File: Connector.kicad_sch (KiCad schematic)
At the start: 1 part, among them J6 2-338069-0

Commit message: Стартовый вариант
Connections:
- net HIN_A: now reaches J6.1
- net LIN_B: now reaches J6.10
- net HIN_B: now reaches J6.11
- net LIN_C: now reaches J6.19
- net LIN_A: now reaches J6.2
- net HIN_C: now reaches J6.20
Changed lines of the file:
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@@
 (kicad_sch (version 20230121) (generator eeschema)
   (paper "A4")
+  (global_label "HIN_C" (shape input) (at 132.08 111.76 180) (fields_autoplaced)
+    (effects (font (size 1.27 1.27)) (justify right))
+    (property "Intersheetrefs" "${INTERSHEET_REFS}" (at 123.5914 111.76 0)
+      (effects (font (size 1.27 1.27)) (justify right) hide)
+    )
+  )
+  (global_label "LIN_B" (shape input) (at 132.08 86.36 180) (fields_autoplaced)
+    (effects (font (size 1.27 1.27)) (justify right))
+    (property "Intersheetrefs" "${INTERSHEET_REFS}" (at 123.8938 86.36 0)
+      (effects (font (size 1.27 1.27)) (justify right) hide)
+    )
+  )
+  (global_label "LIN_C" (shape input) (at 132.08 109.22 180) (fields_autoplaced)
+    (effects (font (size 1.27 1.27)) (justify right))
+    (property "Intersheetrefs" "${INTERSHEET_REFS}" (at 123.8938 109.22 0)
+      (effects (font (size 1.27 1.27)) (justify right) hide)
+    )
+  )
+  (global_label "HIN_A" (shape input) (at 132.08 63.5 180) (fields_autoplaced)
+    (effects (font (size 1.27 1.27)) (justify right))
+    (property "Intersheetrefs" "${INTERSHEET_REFS}" (at 123.7728 63.5 0)
+      (effects (font (size 1.27 1.27)) (justify right) hide)
+    )
+  )
+  (global_label "HIN_B" (shape input) (at 132.08 88.9 180) (fields_autoplaced)
+    (effects (font (size 1.27 1.27)) (justify right))
+    (property "Intersheetrefs" "${INTERSHEET_REFS}" (at 123.5914 88.9 0)
+      (effects (font (size 1.27 1.27)) (justify right) hide)
+    )
+  )
+  (global_label "LIN_A" (shape input) (at 132.08 66.04 180) (fields_autoplaced)
+    (effects (font (size 1.27 1.27)) (justify right))
+    (property "Intersheetrefs" "${INTERSHEET_REFS}" (at 124.0752 66.04 0)
+      (effects (font (size 1.27 1.27)) (justify right) hide)
+    )
+  )
   (symbol (lib_id "Connector_My:2-338069-0") (at 132.08 63.5 0) (unit 1)
     (in_bom yes) (on_board yes) (dnp no) (fields_autoplaced)

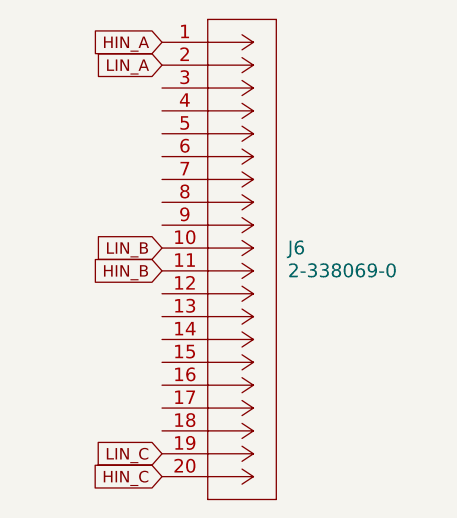
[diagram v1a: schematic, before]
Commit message: Добавил шунты
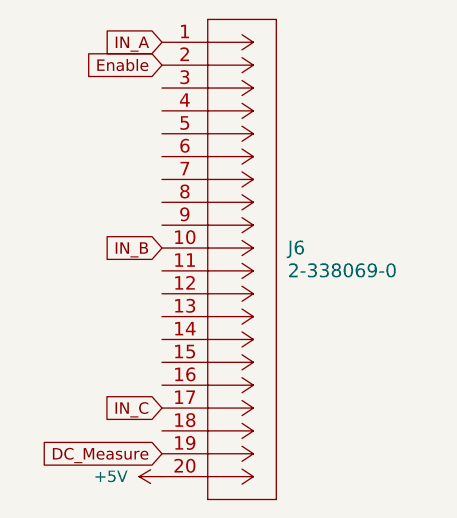
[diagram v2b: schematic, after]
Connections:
- net IN_C: now reaches J6.17
- net HIN_A renamed IN_A
- net HIN_B: no longer names the net of J6.11
- net HIN_C renamed +5V
- net LIN_A renamed Enable
- net LIN_B renamed IN_B
- net LIN_C renamed DC_Measure
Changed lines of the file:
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@@
 (kicad_sch (version 20230121) (generator eeschema)
   (paper "A4")
-  (global_label "HIN_C" (shape input) (at 132.08 111.76 180) (fields_autoplaced)
+  (global_label "DC_Measure" (shape input) (at 132.08 109.22 180) (fields_autoplaced)
     (effects (font (size 1.27 1.27)) (justify right))
-    (property "Intersheetrefs" "${INTERSHEET_REFS}" (at 123.5914 111.76 0)
+    (property "Intersheetrefs" "${INTERSHEET_REFS}" (at 117.8463 109.22 0)
       (effects (font (size 1.27 1.27)) (justify right) hide)
     )
   )
-  (global_label "LIN_B" (shape input) (at 132.08 86.36 180) (fields_autoplaced)
+  (global_label "IN_C" (shape input) (at 132.08 104.14 180) (fields_autoplaced)
     (effects (font (size 1.27 1.27)) (justify right))
-    (property "Intersheetrefs" "${INTERSHEET_REFS}" (at 123.8938 86.36 0)
+    (property "Intersheetrefs" "${INTERSHEET_REFS}" (at 124.9219 104.14 0)
       (effects (font (size 1.27 1.27)) (justify right) hide)
     )
   )
-  (global_label "LIN_C" (shape input) (at 132.08 109.22 180) (fields_autoplaced)
+  (global_label "Enable" (shape input) (at 132.08 66.04 180) (fields_autoplaced)
     (effects (font (size 1.27 1.27)) (justify right))
-    (property "Intersheetrefs" "${INTERSHEET_REFS}" (at 123.8938 109.22 0)
+    (property "Intersheetrefs" "${INTERSHEET_REFS}" (at 122.745 66.04 0)
       (effects (font (size 1.27 1.27)) (justify right) hide)
     )
   )
-  (global_label "HIN_A" (shape input) (at 132.08 63.5 180) (fields_autoplaced)
+  (global_label "IN_A" (shape input) (at 132.08 63.5 180) (fields_autoplaced)
     (effects (font (size 1.27 1.27)) (justify right))
-    (property "Intersheetrefs" "${INTERSHEET_REFS}" (at 123.7728 63.5 0)
+    (property "Intersheetrefs" "${INTERSHEET_REFS}" (at 125.1033 63.5 0)
       (effects (font (size 1.27 1.27)) (justify right) hide)
     )
   )
-  (global_label "HIN_B" (shape input) (at 132.08 88.9 180) (fields_autoplaced)
+  (global_label "IN_B" (shape input) (at 132.08 86.36 180) (fields_autoplaced)
     (effects (font (size 1.27 1.27)) (justify right))
-    (property "Intersheetrefs" "${INTERSHEET_REFS}" (at 123.5914 88.9 0)
+    (property "Intersheetrefs" "${INTERSHEET_REFS}" (at 124.9219 86.36 0)
       (effects (font (size 1.27 1.27)) (justify right) hide)
     )
   )
-  (global_label "LIN_A" (shape input) (at 132.08 66.04 180) (fields_autoplaced)
-    (effects (font (size 1.27 1.27)) (justify right))
-    (property "Intersheetrefs" "${INTERSHEET_REFS}" (at 124.0752 66.04 0)
-      (effects (font (size 1.27 1.27)) (justify right) hide)
+  (symbol (lib_id "power:+5V") (at 132.08 111.76 90) (unit 1)
+    (in_bom yes) (on_board yes) (dnp no) (fields_autoplaced)
+    (property "Reference" "#PWR010" (at 135.89 111.76 0)
+      (effects (font (size 1.27 1.27)) hide)
+    )
+    (property "Value" "+5V" (at 128.27 111.76 90)
+      (effects (font (size 1.27 1.27)) (justify left))
+    )
+    (property "Footprint" "" (at 132.08 111.76 0)
+      (effects (font (size 1.27 1.27)) hide)
+    )
+    (property "Datasheet" "" (at 132.08 111.76 0)
+      (effects (font (size 1.27 1.27)) hide)
+    )
+    (pin "1")
+    (instances
+      (project "Силовая плата"
+        (path "/96c6fc92-8ec6-44f7-b0dc-9ad8f1acea09"
+          (reference "#PWR010") (unit 1)
+        )
+        (path "/96c6fc92-8ec6-44f7-b0dc-9ad8f1acea09/1efb5faf-bb82-4ac6-a144-d6576b4720aa"
+          (reference "#PWR03") (unit 1)
+        )
+        (path "/96c6fc92-8ec6-44f7-b0dc-9ad8f1acea09/a27b443f-c036-4fd6-934c-6ea912709de0"
+          (reference "#PWR09") (unit 1)
+        )
+      )
     )
   )

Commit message: Стартовый вариант
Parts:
- removed J6: 2-338069-0, Connector_My:2-338069-0, symbol Connector_My:2-338069-0

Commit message: Стартовая версия
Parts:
- added J6: Conn_02x04_Odd_Even, Connector_PinHeader_2.54mm:PinHeader_2x04_P2.54mm_Vertical, symbol Connector_Generic:Conn_02x04_Odd_Even
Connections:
- net +12V: now also J6.4 (Pin_4)
- net +5V: now also J6.6 (Pin_6)
- net DC_Measure: now also J6.8 (Pin_8)
- net Enable: now also J6.7 (Pin_7)
- net GND: now also J6.2 (Pin_2)
- net IN_A: now also J6.1 (Pin_1)
- net IN_B: now also J6.3 (Pin_3)
- net IN_C: now also J6.5 (Pin_5)

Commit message: Стартовая версия
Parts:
- removed J6: Conn_02x04_Odd_Even, Connector_PinHeader_2.54mm:PinHeader_2x04_P2.54mm_Vertical, symbol Connector_Generic:Conn_02x04_Odd_Even
- added J6: B_CTRL, Connector_PinSocket_2.54mm:PinSocket_2x02_P2.54mm_Vertical_SMD, symbol Connector_Generic:Conn_02x02_Odd_Even
- added J7: A_CTRL, Connector_PinSocket_2.54mm:PinSocket_2x04_P2.54mm_Vertical_SMD, symbol Connector_Generic:Conn_02x04_Odd_Even
- added J9: C_CTRL, Connector_PinSocket_2.54mm:PinSocket_2x04_P2.54mm_Vertical_SMD, symbol Connector_Generic:Conn_02x04_Odd_Even
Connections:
- net +5V: now also J9.7 (Pin_7)
- net DC_Measure: now also J9.5 (Pin_5)
- net GND: now also J6.4 (Pin_4), J7.4 (Pin_4), J7.6 (Pin_6), J7.8 (Pin_8), J9.4 (Pin_4), J9.6 (Pin_6), J9.8 (Pin_8)
- new net +24V: J7.5 (Pin_5)
- new net A: J7.3 (Pin_3)
- new net B: J6.3 (Pin_3)
- new net C: J9.3 (Pin_3)
- new net G1: J7.1 (Pin_1)
- new net G2: J7.2 (Pin_2)
- new net G3: J6.1 (Pin_1)
- new net G4: J6.2 (Pin_2)
- new net G5: J9.1 (Pin_1)
- new net G6: J9.2 (Pin_2)
- new net Temp_out: J7.7 (Pin_7)

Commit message: Стартовая версия
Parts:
- removed J6: B_CTRL, Connector_PinSocket_2.54mm:PinSocket_2x02_P2.54mm_Vertical_SMD, symbol Connector_Generic:Conn_02x02_Odd_Even
- removed J7: A_CTRL, Connector_PinSocket_2.54mm:PinSocket_2x04_P2.54mm_Vertical_SMD, symbol Connector_Generic:Conn_02x04_Odd_Even
- removed J9: C_CTRL, Connector_PinSocket_2.54mm:PinSocket_2x04_P2.54mm_Vertical_SMD, symbol Connector_Generic:Conn_02x04_Odd_Even
- added J6: Conn_01x04, Connector_PinHeader_2.54mm:PinHeader_1x04_P2.54mm_Vertical, symbol Connector_Generic:Conn_01x04
- added J9: Conn_01x08, Connector_PinHeader_2.54mm:PinHeader_1x08_P2.54mm_Vertical, symbol Connector_Generic:Conn_01x08
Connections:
- net A: now also J6.2 (Pin_2)
- net B: now also J9.8 (Pin_8)
- net C: now also J9.4 (Pin_4)
- net G1: now also J6.1 (Pin_1)
- net G2: now also J6.3 (Pin_3)
- net G3: now also J9.7 (Pin_7)
- net G4: now also J9.5 (Pin_5)
- net G5: now also J9.3 (Pin_3)
- net G6: now also J9.1 (Pin_1)
- net GND: now also J6.4 (Pin_4), J9.2 (Pin_2), J9.6 (Pin_6)

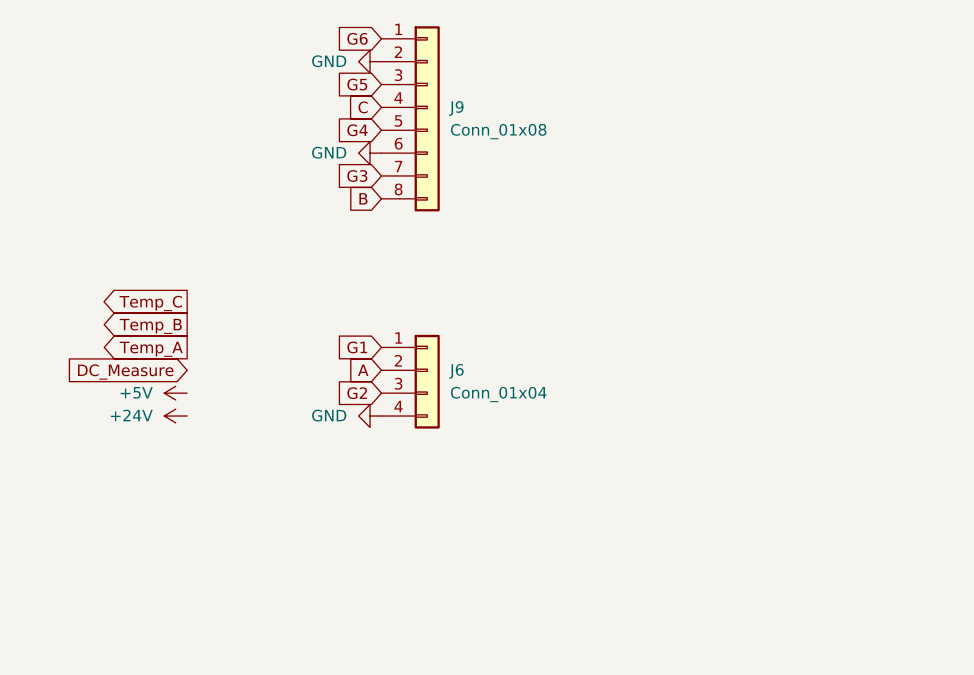
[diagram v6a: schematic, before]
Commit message: Перенес защиту от переполюсовки и добавил керамику
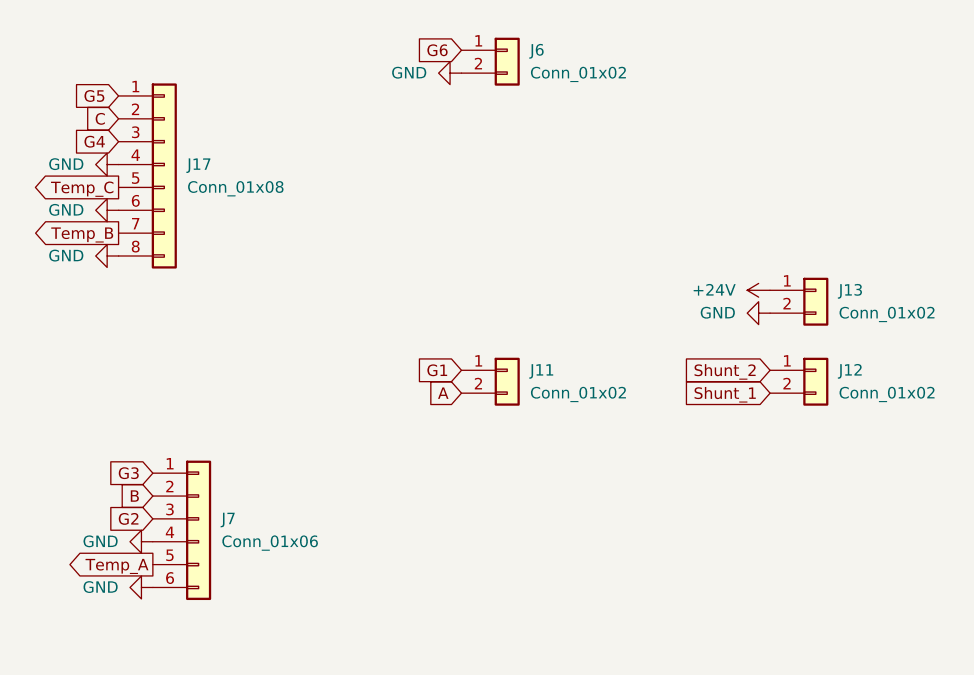
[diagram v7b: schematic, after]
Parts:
- removed J6: Conn_01x04, Connector_PinHeader_2.54mm:PinHeader_1x04_P2.54mm_Vertical, symbol Connector_Generic:Conn_01x04
- removed J9: Conn_01x08, Connector_PinHeader_2.54mm:PinHeader_1x08_P2.54mm_Vertical, symbol Connector_Generic:Conn_01x08
- added J11, J12, J13, J6: Conn_01x02, Connector_PinHeader_2.54mm:PinHeader_1x02_P2.54mm_Vertical_SMD_Pin1Left, symbol Connector_Generic:Conn_01x02
- added J17: Conn_01x08, Connector_PinHeader_2.54mm:PinHeader_1x08_P2.54mm_Vertical_SMD_Pin1Left, symbol Connector_Generic:Conn_01x08
- added J7: Conn_01x06, Connector_PinHeader_2.54mm:PinHeader_1x06_P2.54mm_Vertical_SMD_Pin1Left, symbol Connector_Generic:Conn_01x06
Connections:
- net +24V: now also J13.1 (Pin_1)
- net A: now also J11.2 (Pin_2)
- net B: now also J7.2 (Pin_2)
- net C: now also J17.2 (Pin_2)
- net G1: now also J11.1 (Pin_1)
- net G2: now also J7.3 (Pin_3)
- net G3: now also J7.1 (Pin_1)
- net G4: now also J17.3 (Pin_3)
- net G5: now also J17.1 (Pin_1)
- net G6: now also J6.1 (Pin_1)
- net GND: now also J13.2 (Pin_2), J17.4 (Pin_4), J17.6 (Pin_6), J17.8 (Pin_8), J6.2 (Pin_2), J7.4 (Pin_4), J7.6 (Pin_6)
- net Temp_A: now also J7.5 (Pin_5)
- net Temp_B: now also J17.7 (Pin_7)
- net Temp_C: now also J17.5 (Pin_5)
- new net Shunt_1: J12.2 (Pin_2)
- new net Shunt_2: J12.1 (Pin_1)

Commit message: Поставил керамические Y конденсаторы
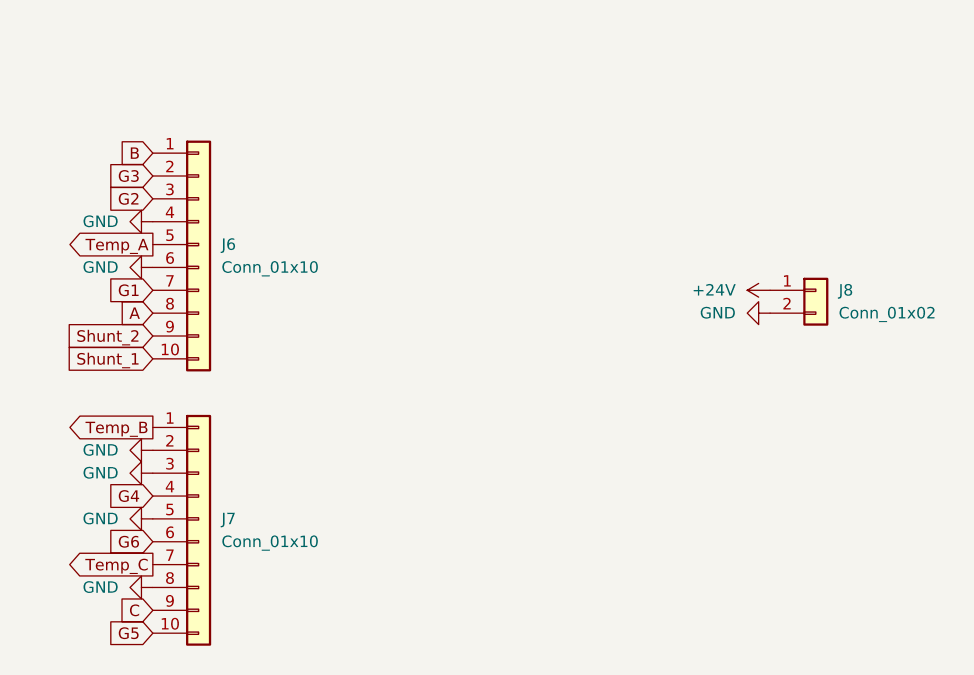
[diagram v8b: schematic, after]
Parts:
- removed J11, J12, J6: Conn_01x02, Connector_PinHeader_2.54mm:PinHeader_1x02_P2.54mm_Vertical_SMD_Pin1Left, symbol Connector_Generic:Conn_01x02
- removed J17: Conn_01x08, Connector_PinHeader_2.54mm:PinHeader_1x08_P2.54mm_Vertical_SMD_Pin1Left, symbol Connector_Generic:Conn_01x08
- removed J7: Conn_01x06, Connector_PinHeader_2.54mm:PinHeader_1x06_P2.54mm_Vertical_SMD_Pin1Left, symbol Connector_Generic:Conn_01x06
- added J6, J7: Conn_01x10, Connector_PinHeader_2.54mm:PinHeader_1x10_P2.54mm_Vertical, symbol Connector_Generic:Conn_01x10
- renumbered J13 to J8
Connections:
- net A: now also J6.8 (Pin_8)
- net B: now also J6.1 (Pin_1)
- net C: now also J7.9 (Pin_9)
- net G1: now also J6.7 (Pin_7)
- net G2: now also J6.3 (Pin_3)
- net G3: now also J6.2 (Pin_2)
- net G4: now also J7.4 (Pin_4)
- net G5: now also J7.10 (Pin_10)
- net G6: now also J7.6 (Pin_6)
- net GND: now also J6.4 (Pin_4), J6.6 (Pin_6), J7.2 (Pin_2), J7.3 (Pin_3), J7.5 (Pin_5), J7.8 (Pin_8)
- net Shunt_1: now also J6.10 (Pin_10)
- net Shunt_2: now also J6.9 (Pin_9)
- net Temp_A: now also J6.5 (Pin_5)
- net Temp_B: now also J7.1 (Pin_1)
- net Temp_C: now also J7.7 (Pin_7)
